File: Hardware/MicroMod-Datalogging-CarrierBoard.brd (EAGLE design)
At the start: 61 x 40.6 mm, 127 parts, among them J11 microSD, J12 SPI, J14 I2C, J2 JTAG, J3 QWIIC_RIGHT_ANGLE, J5 UART, J6 MICROMOD-2222-C, J8 Dedicated, Q2 20V/4.2A/52mΩ/1.4W, Q4 20V/4.2A/52mΩ/1.4W, U2 MCP73831, U5 AP7361C-33FGE

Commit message: Update v-reg device
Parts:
- U5: value AP7361C-33FGE -> AP7361C-33; device ublox:8-UDFN -> SparkFun-IC-Power:UDFN-8
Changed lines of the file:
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@@
 <layer number="44" name="Drills" color="7" fill="1" visible="no" active="yes"/>
 <layer number="45" name="Holes" color="7" fill="1" visible="yes" active="yes"/>
-<layer number="46" name="Milling" color="3" fill="1" visible="yes" active="yes"/>
+<layer number="46" name="Milling" color="3" fill="1" visible="no" active="yes"/>
 <layer number="47" name="Measures" color="7" fill="1" visible="no" active="yes"/>
 <layer number="48" name="Document" color="7" fill="1" visible="no" active="yes"/>
@@
 <attribute name="VALUE" x="8.182" y="7.62" size="0.6096" layer="27" font="vector" ratio="20" rot="R90" align="top-center"/>
 </element>
-<element name="U5" library="ublox" package="8-UDFN" value="AP7361C-33FGE" x="10.16" y="10.16" smashed="yes">
+<element name="U5" library="SparkFun-IC-Power" package="UDFN-8" value="AP7361C-33" x="10.16" y="10.16" smashed="yes">
 <attribute name="NAME" x="8.46" y="10.16" size="0.6096" layer="25" font="vector" ratio="20" rot="R90" align="bottom-center"/>
 <attribute name="PROD_ID" value="VREG-14094" x="10.16" y="11.43" size="1.778" layer="27" font="vector" ratio="15" display="off"/>
@@
 <via x="44.45" y="34.925" extent="1-16" drill="0.3048"/>
 <via x="42.037" y="11.049" extent="1-16" drill="0.3048"/>
-<wire x1="55.35" y1="22.49" x2="59" y2="32.65" width="0" layer="19" extent="1-1"/>
-<wire x1="53.721" y1="22.479" x2="55.35" y2="22.49" width="0" layer="19" extent="1-1"/>
-<wire x1="58" y1="19.5" x2="55.35" y2="22.49" width="0" layer="19" extent="1-1"/>
-<wire x1="50.38" y1="17.78" x2="53.721" y2="22.479" width="0" layer="19" extent="1-1"/>
-<wire x1="50.419" y1="16.51" x2="50.38" y2="17.78" width="0" layer="19" extent="1-1"/>
-<wire x1="44.85" y1="21.1" x2="50.38" y2="17.78" width="0" layer="19" extent="1-1"/>
-<wire x1="44.069" y1="14.986" x2="44.85" y2="21.1" width="0" layer="19" extent="1-1"/>
-<wire x1="42.037" y1="11.049" x2="44.069" y2="14.986" width="0" layer="19" extent="1-1"/>
-<wire x1="43.18" y1="9.74" x2="42.037" y2="11.049" width="0" layer="19" extent="1-1"/>
-<wire x1="44.45" y1="9.74" x2="43.18" y2="9.74" width="0" layer="19" extent="1-1"/>
-<wire x1="45.72" y1="10.287" x2="44.45" y2="9.74" width="0" layer="19" extent="1-1"/>
-<wire x1="44.45" y1="1.27" x2="44.45" y2="9.74" width="0" layer="19" extent="1-1"/>
-<wire x1="55.88" y1="9.93" x2="50.419" y2="16.51" width="0" layer="19" extent="1-1"/>
-<wire x1="55.118" y1="8.89" x2="55.88" y2="9.93" width="0" layer="19" extent="1-1"/>
-<wire x1="34.29" y1="1.27" x2="44.45" y2="1.27" width="0" layer="19" extent="1-1"/>
-<wire x1="32.004" y1="1.905" x2="34.29" y2="1.27" width="0" layer="19" extent="1-1"/>
-<wire x1="26.416" y1="1.905" x2="32.004" y2="1.905" width="0" layer="19" extent="1-1"/>
-<wire x1="24.384" y1="1.905" x2="26.416" y2="1.905" width="0" layer="19" extent="1-1"/>
-<wire x1="18.796" y1="1.905" x2="24.384" y2="1.905" width="0" layer="19" extent="1-1"/>
-<wire x1="16.51" y1="2.921" x2="18.796" y2="1.905" width="0" layer="19" extent="1-1"/>
-<wire x1="15.24" y1="2.921" x2="16.51" y2="2.921" width="0" layer="19" extent="1-1"/>
-<wire x1="13.97" y1="2.921" x2="15.24" y2="2.921" width="0" layer="19" extent="1-1"/>
-<wire x1="16.51" y1="4.23" x2="16.51" y2="2.921" width="0" layer="19" extent="1-1"/>
-<wire x1="15.24" y1="4.23" x2="16.51" y2="4.23" width="0" layer="19" extent="1-1"/>
-<wire x1="13.97" y1="4.23" x2="15.24" y2="4.23" width="0" layer="19" extent="1-1"/>
-<wire x1="15.748" y1="8.763" x2="15.24" y2="4.23" width="0" layer="19" extent="1-1"/>
-<wire x1="14.605" y1="9.01" x2="15.748" y2="8.763" width="0" layer="19" extent="1-1"/>
-<wire x1="17.272" y1="9.779" x2="15.748" y2="8.763" width="0" layer="19" extent="1-1"/>
-<wire x1="18.855" y1="9.8" x2="17.272" y2="9.779" width="0" layer="19" extent="1-1"/>
-<wire x1="18.855" y1="11.3" x2="18.855" y2="9.8" width="0" layer="19" extent="1-1"/>
-<wire x1="11.43" y1="10.16" x2="14.605" y2="9.01" width="0" layer="19" extent="1-1"/>
-<wire x1="10.16" y1="10.16" x2="11.43" y2="10.16" width="0" layer="19" extent="1-1"/>
-<wire x1="8.89" y1="10.16" x2="10.16" y2="10.16" width="0" layer="19" extent="1-1"/>
-<wire x1="11.135" y1="8.785" x2="11.43" y2="10.16" width="0" layer="19" extent="1-1"/>
-<wire x1="11.049" y1="7.747" x2="11.135" y2="8.785" width="0" layer="19" extent="1-1"/>
-<wire x1="7.62" y1="6.77" x2="11.049" y2="7.747" width="0" layer="19" extent="1-1"/>
-<wire x1="7.62" y1="5.461" x2="7.62" y2="6.77" width="0" layer="19" extent="1-1"/>
-<wire x1="7.62" y1="13.55" x2="8.89" y2="10.16" width="0" layer="19" extent="1-1"/>
-<wire x1="7.62" y1="14.859" x2="7.62" y2="13.55" width="0" layer="19" extent="1-1"/>
-<wire x1="11.01" y1="15.24" x2="7.62" y2="14.859" width="0" layer="19" extent="1-1"/>
-<wire x1="12.192" y1="15.24" x2="11.01" y2="15.24" width="0" layer="19" extent="1-1"/>
-<wire x1="11.01" y1="13.97" x2="11.01" y2="15.24" width="0" layer="19" extent="1-1"/>
-<wire x1="11.811" y1="17.78" x2="12.192" y2="15.24" width="0" layer="19" extent="1-1"/>
-<wire x1="10.29" y1="17.78" x2="11.811" y2="17.78" width="0" layer="19" extent="1-1"/>
-<wire x1="15.24" y1="14.39" x2="12.192" y2="15.24" width="0" layer="19" extent="1-1"/>
-<wire x1="16.637" y1="14.224" x2="15.24" y2="14.39" width="0" layer="19" extent="1-1"/>
-<wire x1="17.145" y1="17.907" x2="16.637" y2="14.224" width="0" layer="19" extent="1-1"/>
-<wire x1="17.145" y1="19.304" x2="17.145" y2="17.907" width="0" layer="19" extent="1-1"/>
-<wire x1="17.145" y1="20.828" x2="17.145" y2="19.304" width="0" layer="19" extent="1-1"/>
-<wire x1="18.855" y1="20.8" x2="17.145" y2="20.828" width="0" layer="19" extent="1-1"/>
-<wire x1="18.855" y1="19.3" x2="18.855" y2="20.8" width="0" layer="19" extent="1-1"/>
-<wire x1="18.855" y1="17.8" x2="18.855" y2="19.3" width="0" layer="19" extent="1-1"/>
-<wire x1="14.732" y1="22.86" x2="17.145" y2="20.828" width="0" layer="19" extent="1-1"/>
-<wire x1="14.82" y1="24.13" x2="14.732" y2="22.86" width="0" layer="19" extent="1-1"/>
-<wire x1="16.51" y1="28.79" x2="14.82" y2="24.13" width="0" layer="19" extent="1-1"/>
-<wire x1="17.145" y1="29.845" x2="16.51" y2="28.79" width="0" layer="19" extent="1-1"/>
-<wire x1="18.855" y1="28.3" x2="17.145" y2="29.845" width="0" layer="19" extent="1-1"/>
-<wire x1="13.97" y1="29.2401" x2="16.51" y2="28.79" width="0" layer="19" extent="1-1"/>
-<wire x1="12.7" y1="32.6" x2="13.97" y2="29.2401" width="0" layer="19" extent="1-1"/>
-<wire x1="11.43" y1="32.512" x2="12.7" y2="32.6" width="0" layer="19" extent="1-1"/>
-<wire x1="7.51" y1="26.94" x2="11.43" y2="32.512" width="0" layer="19" extent="1-1"/>
-<wire x1="7.493" y1="25.654" x2="7.51" y2="26.94" width="0" layer="19" extent="1-1"/>
-<wire x1="2.54" y1="26.67" x2="7.51" y2="26.94" width="0" layer="19" extent="1-1"/>
-<wire x1="26.405" y1="18.55" x2="18.855" y2="19.3" width="0" layer="19" extent="1-1"/>
-<wire x1="27.94" y1="18.415" x2="26.405" y2="18.55" width="0" layer="19" extent="1-1"/>
-<wire x1="31.115" y1="17.78" x2="27.94" y2="18.415" width="0" layer="19" extent="1-1"/>
-<wire x1="31.115" y1="16.51" x2="31.115" y2="17.78" width="0" layer="19" extent="1-1"/>
-<wire x1="31.115" y1="13.97" x2="31.115" y2="16.51" width="0" layer="19" extent="1-1"/>
-<wire x1="7.62" y1="39.37" x2="11.43" y2="32.512" width="0" layer="19" extent="1-1"/>
-<wire x1="47.59" y1="34.98" x2="59" y2="32.65" width="0" layer="19" extent="1-1"/>
-<wire x1="44.45" y1="34.925" x2="47.59" y2="34.98" width="0" layer="19" extent="1-1"/>
-<wire x1="31.75" y1="39.37" x2="44.45" y2="34.925" width="0" layer="19" extent="1-1"/>
-<wire x1="29.21" y1="39.37" x2="31.75" y2="39.37" width="0" layer="19" extent="1-1"/>
-<wire x1="26.67" y1="39.37" x2="29.21" y2="39.37" width="0" layer="19" extent="1-1"/>
 </signal>
 <signal name="3.3V">

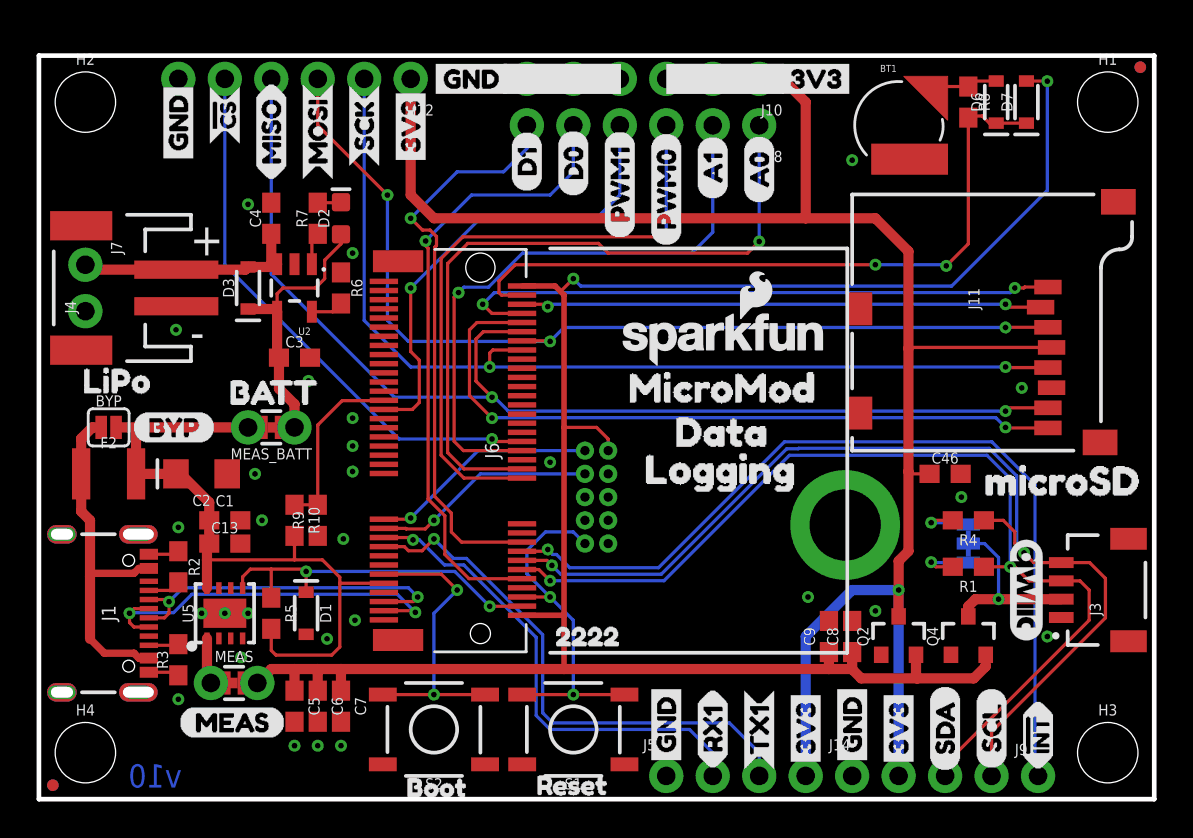
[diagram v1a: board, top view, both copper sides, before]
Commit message: Change peripheral power to regulators. Upgrade buzzard labels. Add VE jumper.
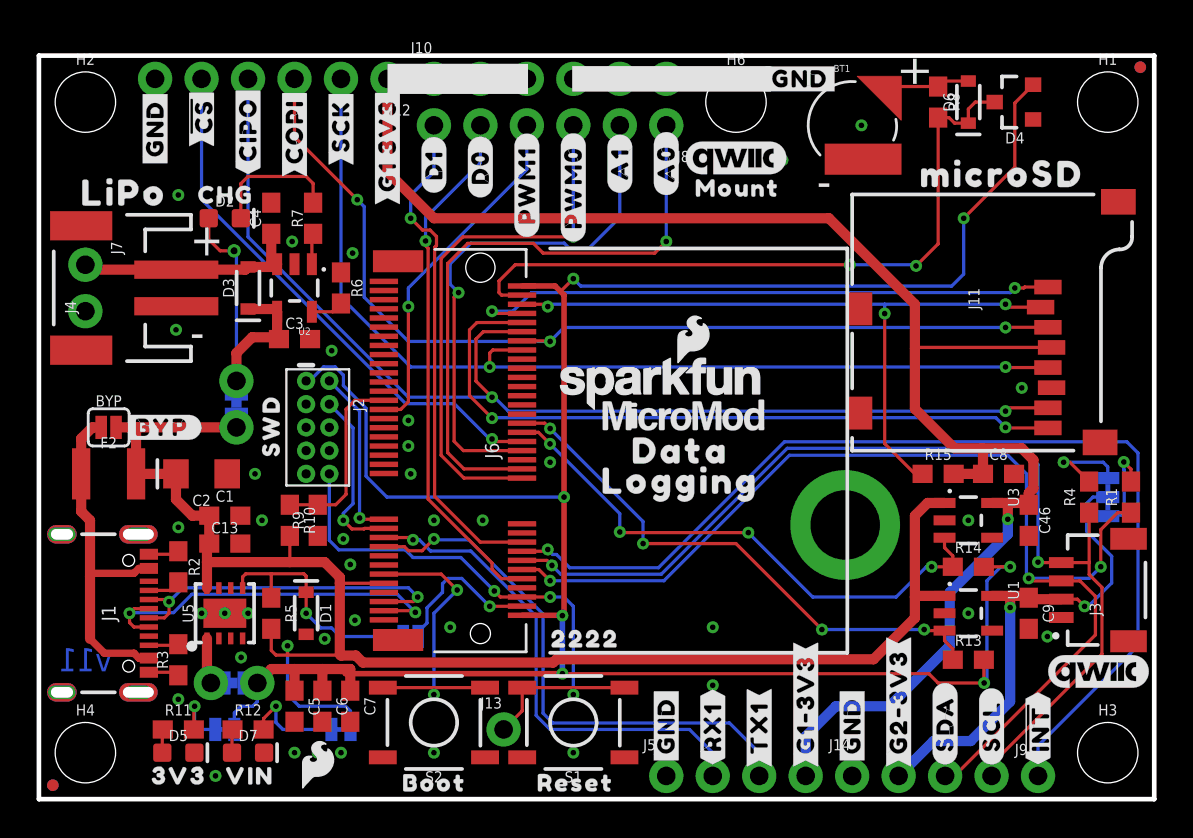
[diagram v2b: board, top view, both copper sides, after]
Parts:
- removed Q2, Q4: 20V/4.2A/52mΩ/1.4W, SparkFun-DiscreteSemi:SOT23-3
- removed U$43, U$44: (no value), buzzard_labels (12):A00
- removed U$45, U$53, U$54: (no value), SparkFun-Buzzard:GND_P
- removed U$46: (no value), SparkFun-Buzzard:3V3_P
- removed U$47: (no value), SparkFun-Buzzard:SDA_IO
- removed U$48: (no value), SparkFun-Buzzard:SCL_IO
- removed U$49: (no value), SparkFun-Buzzard:SCK_O
- removed U$52: (no value), SparkFun-Buzzard:!CS_O
- removed U$55: (no value), buzzard_labels (9):22229
- removed U$56: (no value), buzzard_labels:BATT0
- removed U$57, U$58: (no value), buzzard_labels (1):A10
- removed U$59, U$60: (no value), buzzard_labels (1):PWM01
- removed U$61: (no value), buzzard_labels (10):PWM10
- added 3V3_LED, VIN_LED: (no value), SparkFun-Jumpers:SMT-JUMPER_2_NC_TRACE_SILK
- added D4: BAS70-05, SparkFun-DiscreteSemi:SOT23-3
- added D5: RED, SparkFun-LED:LED-0603
- added H6: STAND-OFF, SparkFun-Hardware:STAND-OFF
- added J13: (no value), SparkFun-Connectors:1X01_NO_SILK
- added LOGO5: QWIIC_LOGO_CONNECTOR, SparkFun-Aesthetics:QWIIC_5.5MM
- added R11: 1k, SparkFun-Resistors:0603
- added R12: 4.7k, SparkFun-Resistors:0603
- added R13, R14, R15: 100k, SparkFun-Resistors:0603
- added U$62: (no value), SparkFun-MicroMod:MICROMOD_MI_LOGO_.35
- added U$63: (no value), SparkFun-MicroMod:MICROMOD_LOGO_.35
- added U$65: (no value), output:#G1_3V3#0
- added U$66: (no value), SparkFun-Aesthetics:SFE_LOGO_FLAME_.1
- added U$72, U$73: (no value), output:#COPI#0
- added U$76: (no value), output:#D1#0
- added U$77: (no value), output:#D0#0
- added U$78: (no value), output:#A0#3
- added U$79: (no value), output:#A1#2
- added U$80: (no value), output:#PWM0#0
- added U$81: (no value), output:#PWM1#1
- added U$82: (no value), output:##INT##6
- added U$83: (no value), output:#G2#3V3#3
- added U$86: (no value), output:#RX1#1
- added U$87: (no value), output:#SCL#5
- added U$88: (no value), output:#SDA#4
- added U$89: (no value), output:#TX1#2
- added U$90: (no value), output:#G1#3V3#0
- added U$91: (no value), output:BOOT0
- added U$92: (no value), output:RESET1
- added U$93: (no value), output:3V30
- added U$94: (no value), output:VIN1
- added U$95: (no value), output:#BYP#3
- added U$96: (no value), output:CHG1
- added U$97: (no value), output:SWD0
- added U1, U3: 3.3V, SparkFun-IC-Power:SOT23-5
- added VE: (no value), SparkFun-Jumpers:SMT-JUMPER_2_NO_SILK
- C8: value 10uF -> 1.0uF
- D7: value 1A/23V/620mV -> Yellow; device SparkFun-DiscreteSemi:SOD-323 -> SparkFun-LED:LED-0603
- R8: value 1k -> 3.3k
- U$1: device SparkFun-Buzzard:3V3_P -> SparkFun-Aesthetics:SFE_LOGO_FLAME_.1
- U$10: device SparkFun-Buzzard:!CS_O -> output:#PWM0#0
- U$11: device SparkFun-Buzzard:GND_P -> output:MICROSD0
- U$12: device buzzard_labels (12):D13 -> output:#A1#2
- U$13: device buzzard_labels (12):D13 -> output:#A0#3
- U$14: device buzzard_labels (12):D02 -> output:MOUNT0
- U$15: device buzzard_labels (10):PWM10 -> output:LIPO0
- U$16: device buzzard_labels (12):D02 -> output:DATA0
- U$17: device SparkFun-Buzzard:3V3_P -> output:#RX1#1
- U$18: device SparkFun-Buzzard:JTAG_TO -> output:#GND#0
- U$19: device buzzard_labels (10):BOOT2 -> output:LOGGING1
- U$2: device buzzard_labels (9):RESET3 -> output:#D1#0
- U$20: device SparkFun-Buzzard:3V3_P -> output:22220
- U$21: device SparkFun-Buzzard:!INT_I -> output:#TX1#2
- U$22: device buzzard_labels (9):LOGGING4 -> output:#I2C#0
- U$23: device SparkFun-Buzzard:3V3_P -> output:DATA0
- U$24: device buzzard_labels (11):MICROMOD0 -> output:#GND#0
- U$25: device buzzard_labels (6):RX10 -> output:#G1#3V3#0
- U$26: device SparkFun-Buzzard:3V3_P -> output:LOGGING1
- U$27: device SparkFun-Buzzard:BYP -> output:#GND#0
- U$28: device buzzard_labels (10):MICROSD4 -> output:#MEAS#3
- U$29: device buzzard_labels (6):RX10 -> output:#G2#3V3#3
- U$3: device SparkFun-Buzzard:3V3_P -> output:#D0#0
- U$30: device buzzard_labels (9):DATA3 -> output:#RST#0
- U$31: device buzzard_labels (6):TX13 -> output:#SDA#4
- U$32, U$36, U$42, U$6: device SparkFun-Buzzard:GND_P -> output:#GND#0
- U$33: device buzzard_labels (9):LIPO0 -> output:#VIN#1
- U$34: device buzzard_labels (9):LOGGING4 -> output:#GND#0
- U$35: device SparkFun-Buzzard:!INT_I -> output:#SCL#5
- U$37: device SparkFun-Buzzard:I2C -> SparkFun-MicroMod:MICROMOD_LOGO_.35
- U$38: device SparkFun-Buzzard:3V3_P -> output:##INT##6
- U$39: device SparkFun-Buzzard:SDA_IO -> output:#CIPO#0
- U$4: device buzzard_labels (9):DATA3 -> output:#3V3#2
- U$40: device SparkFun-Buzzard:SCL_IO -> output:#CIPO#0
- U$41: device buzzard_labels (6):TX13 -> output:#VE#0
- U$5: device SparkFun-Buzzard:MEAS -> output:#BATT#0
- U$50: device SparkFun-Buzzard:MOSI_O -> output:##CS##0
- U$51: device SparkFun-Buzzard:MISO_I -> output:##CS##0
- U$64: device buzzard_labels (11):MICROMOD0 -> output:#G1_3V3#0
- U$7: device SparkFun-Buzzard:MOSI_O -> output:#SCK#0
- U$8: device SparkFun-Buzzard:MISO_I -> output:#SCK#0
- U$9: device SparkFun-Buzzard:SCK_O -> output:#PWM1#1
- moved D7 55.4 mm to (11.4, 2.54), turned to 0 degrees
- moved U$40 52.0 mm to (11.4, 34.2), flipped to the bottom
- moved U$39 50.2 mm to (11.4, 34.2)
- moved U$1 45.4 mm to (2.54, 22.9)
- moved U$42 38.1 mm to (39.4, 39.4), flipped to the top, turned to 0 degrees
- moved U$28 37.9 mm to (13.6, 8.13), flipped to the bottom
- moved U$27 34.6 mm to (34.3, 1.78), flipped to the bottom, turned to 90 degrees
- moved U$18 33.9 mm to (6.35, 34.4)
- moved U$2 32.7 mm to (21.6, 33.1), flipped to the bottom, turned to 90 degrees
- moved U$22 30.8 mm to (58.4, 17.9), turned to 90 degrees
- moved U$15 30.6 mm to (1.27, 33.1), turned to 0 degrees
- moved U$11 26.4 mm to (47.1, 34.2)
- moved U$37 25.4 mm to (29.2, 21.1), turned to 0 degrees
- moved U$34 24.7 mm to (43.9, 39.4), flipped to the bottom
- moved U$4 24.5 mm to (9.27, 3.81)
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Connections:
- removed net PERIPHERAL_PWR: Q2.1
- removed net SPI_MISO: J11.DO, J12.4, J6.64
- removed net SPI_MOSI: J11.DI, J12.3, J6.62
- new net 3.3V_EN_VE: D1.C, R5.1, U5.5, VE.2
- new net N$5: D5.A, R11.1
- new net N$6: 3V3_LED.1, R11.2
- new net N$8: R12.2, VIN_LED.1
- new net N$9: D7.A, R12.1
- new net PERIPHERAL_PWR_CTRL: J6.42, R14.1, U3.3
- new net SPI_CIPO: J11.DO/DAT0, J12.4, J6.64
- new net SPI_COPI: J11.DI/CMD, J12.3, J6.62
- net !RESET!: now also J13.1
- net 3.3V: now also 3V3_LED.2, D4.2, R13.2, R14.2; no longer C8.1, C9.1, D7.A, Q2.2, Q4.2
- net 3.3V_EN: now also VE.1; no longer D1.C, R5.1, U5.5
- net 3.3V_LP: now also C8.1, R15.2, U3.5; no longer J14.2, Q2.3
- net GND: now also D5.C, D7.C, U1.2, U3.2
- net QWIIC_PWR: now also C9.1, J14.2, U1.5; no longer Q4.3
- net QWIIC_PWR_CTRL: now also J6.44, R13.1, U1.3; no longer Q4.1
- net RTC_3V: now also D4.3; no longer D7.C
- net SD_!CS!: now also J11.CS/DAT3, R15.1; no longer J11.CS
- net SD_DAT1: now also J11.DAT1; no longer J11.RSV2
- net SD_DAT2: now also J11.DAT2; no longer J11.RSV1
- net VIN: now also U1.1, U3.1, VIN_LED.2
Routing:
- net SPI_CIPO: track 0.00 -> 62.7 mm, vias 0 -> 2
- net SPI_MISO: track 62.6 -> 0.00 mm, vias 2 -> 0
- net SPI_COPI: track 0.00 -> 53.8 mm, vias 0 -> 3
- net SPI_MOSI: track 53.2 -> 0.00 mm, vias 3 -> 0
- net VIN: track 40.3 -> 90.1 mm, vias 0 -> 1
- net PERIPHERAL_PWR_CTRL: track 0.00 -> 30.3 mm, vias 0 -> 4
- net QWIIC_PWR_CTRL: track 0.00 -> 30.3 mm, vias 0 -> 4
- net 3.3V: track 113.6 -> 138.8 mm, vias 2 -> 7
- net QWIIC_PWR: track 10.0 -> 27.1 mm, vias 1 -> 2
- net 3.3V_EN_VE: track 0.00 -> 13.4 mm, vias 0 -> 1
- net !RESET!: track 19.9 -> 32.0 mm, vias 2 -> 3
- net 3.3V_EN: track 19.6 -> 8.54 mm, vias 2 -> 1
- net SD_!CS!: track 28.5 -> 38.9 mm, vias 2 -> 3
- net I2C_!INT!: track 48.3 -> 57.1 mm
- net 3.3V_LP: track 102.5 -> 94.2 mm
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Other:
- board text added: "N. Seidle"
- board text added: "v11"
- board text removed: "v10"

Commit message: Update MicroMod connector with new SPI port assignments.
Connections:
- net SD_!CS!: now also J6.55; no longer J6.70
- net SD_DAT1: no longer J6.66
- net SD_DAT2: no longer J6.68
- net SPI_CIPO: now also J6.61; no longer J6.64
- net SPI_COPI: now also J6.59; no longer J6.62
- net SPI_SCK: now also J6.57; no longer J6.60
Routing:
- net SD_DAT1: track 39.0 -> 0.00 mm, vias 2 -> 0
- net SD_DAT2: track 32.7 -> 0.00 mm, vias 2 -> 0
- net SD_!CS!: track 38.9 -> 52.1 mm
- net SPI_CIPO: track 62.7 -> 58.5 mm, vias 2 -> 3
- net PWM1: track 19.3 -> 22.3 mm
- net SPI_SCK: track 54.8 -> 53.5 mm
- net PWM0: track 29.5 -> 28.5 mm
- net A0: track 34.0 -> 33.0 mm
- net A1: track 29.5 -> 28.5 mm
- net SPI_COPI: track 53.8 -> 54.1 mm, vias 3 -> 4
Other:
- board text added: "v12"
- board text removed: "v11"

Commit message: Change SD to pure SPI connection.
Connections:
- removed net SD_DAT1: J11.DAT1
- removed net SD_DAT2: J11.DAT2
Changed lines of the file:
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@@
 </elements>
 <signals>
-<signal name="SD_DAT1">
-<contactref element="J11" pad="DAT1"/>
-</signal>
 <signal name="SPI_SCK">
 <contactref element="J11" pad="SCLK"/>
@@
 <wire x1="21.336" y1="25.908" x2="20.32" y2="25.908" width="0.1778" layer="1"/>
 </signal>
-<signal name="SD_DAT2">
-<contactref element="J11" pad="DAT2"/>
-</signal>
 <signal name="GND">
